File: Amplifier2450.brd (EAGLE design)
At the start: 39.4 x 35.5 mm, 25 parts, among them IC1 7805DT, Q1 P-KANAL_MOSFET_, X1 SMA-142-0701-801/806, X2 SMA-142-0701-801/806

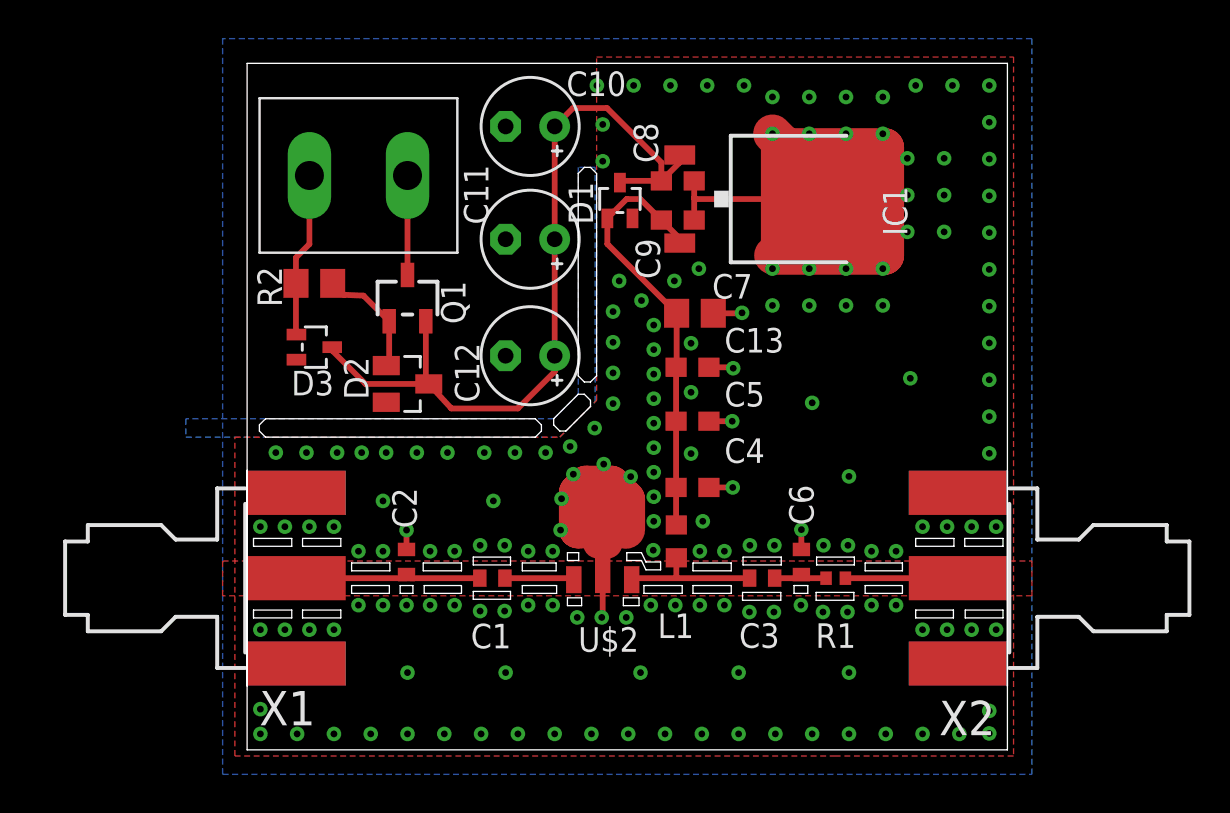
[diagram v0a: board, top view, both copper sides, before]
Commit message: (Tobias): started to apply changes from robert 1st meeting
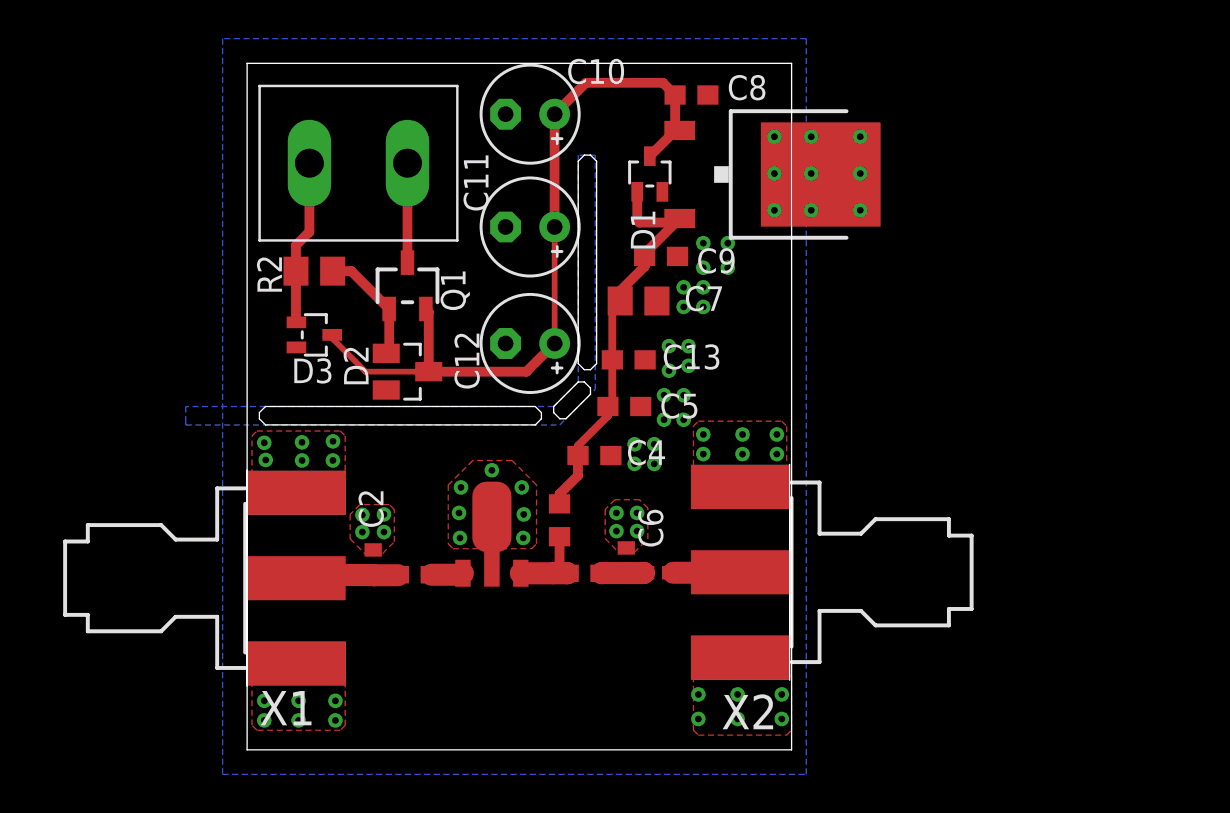
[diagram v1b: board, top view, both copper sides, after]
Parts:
- C13: value 47n -> 22n
- moved X2 11.3 mm to (28.1, 9.19)
- moved R1 9.20 mm to (21.3, 9.17)
- moved C3 9.20 mm to (17.5, 9.14)
- moved C6 9.07 mm to (19.6, 9.80)
- moved L1 6.14 mm to (16.2, 11.9)
- moved U$2 5.75 mm to (12.7, 11.1)
- moved C4 5.34 mm to (18.0, 15.2)
- moved C8 4.50 mm to (23.0, 33.9)
- moved C1 4.02 mm to (8.69, 9.07)
- moved C5 3.61 mm to (19.5, 17.8)
- moved C13 3.32 mm to (19.8, 20.2)
- moved C7 2.99 mm to (20.3, 23.2)
- moved D1 2.07 mm to (20.9, 29.8)
- moved C9 2.07 mm to (21.4, 25.6)
- moved C2 1.73 mm to (6.53, 9.70)
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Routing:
- net GND: track 58.0 -> 8.54 mm, vias 175 -> 59
- net N$2: track 9.75 -> 5.78 mm
- net N$1: track 7.19 -> 4.79 mm
- net +15V: track 41.8 -> 39.4 mm
- net N$5: track 5.82 -> 3.48 mm
- net N$3: track 3.60 -> 1.66 mm
- net +5V: track 22.6 -> 20.9 mm
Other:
- board size 39.4 x 35.5 mm -> 28.2 x 35.5 mm
- board text added: "?????????? Can we use a different width for the power line, so that it has a different impedance and RF will not go up the power line because it would be reflected."
- board text removed: "Lots of vias around the DC-DC Converter gound. This will not only increase the electrical conductance, but also the thermal one. Making use of both ground planes and effectivelly useing them as a heat sink."
- board text removed: "Some random vias in the middle of larger ground planes to make sure that there is no potential difference and the ground is well defined"
- board text removed: "Use thermals around the signal connectors/pads to minimize thermal coupling with other devices"
- board text removed: "Vias at the outer edges intended as shielding from external electro magnetic fields"

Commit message: (Tobias): halfway applied Roberts feedback
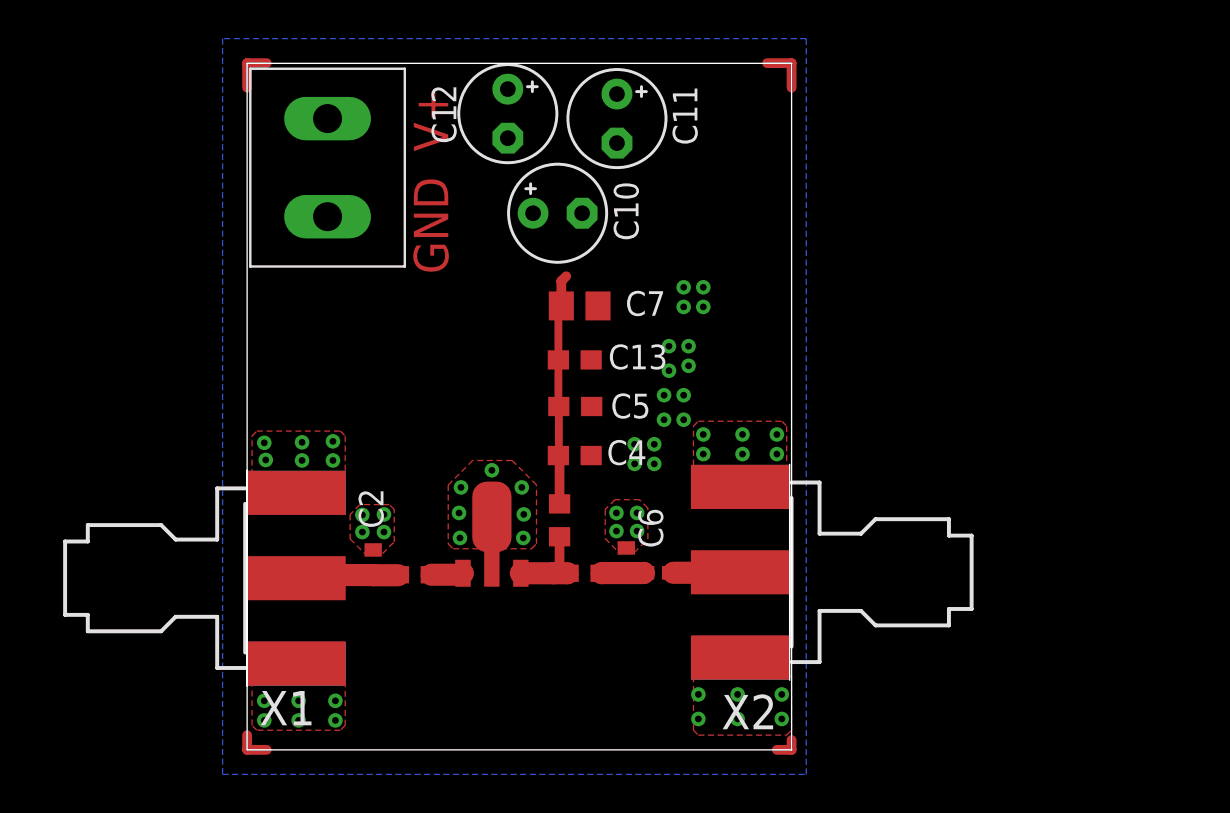
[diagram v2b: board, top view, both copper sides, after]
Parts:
- removed C8: 330n, rcl:C0603
- removed C9: 100n, rcl:C0603
- removed D1, D3: SCHOTTKY_DIODE_, own_htl3r-discrete-1:SOT323
- removed D2: 5,1V, diode:SOT23
- removed IC1: 7805DT, linear:TO252
- removed Q1: P-KANAL_MOSFET_, own_htl3r-discrete-1:SOT346-R
- removed R2: 4k7, rcl:R0805
- C3: value 20p -> 15p
- L1: value 15n -> 72nH
- moved C12 12.0 mm to (13.5, 32.9), turned to 270 degrees
- moved C11 7.19 mm to (19.2, 32.7), turned to 270 degrees
- moved C10 5.32 mm to (16.1, 27.8), turned to 0 degrees
- moved C7 3.06 mm to (17.2, 23.0)
- moved C13 2.79 mm to (17.0, 20.2)
- moved C5 2.54 mm to (17.0, 17.8)
- moved U$1 1.62 mm to (4.17, 30.1), turned to 90 degrees
- moved C4 1.02 mm to (17.0, 15.2)
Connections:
- removed net +15V: C10.+, C11.+, C12.+, C8.1, D1.3, D2.3, D3.3, IC1.1, Q1.2
- removed net N$6: Q1.3, U$1.P$2
- removed net N$7: D2.1, Q1.1, R2.2
- net +5V: now also C10.+, C11.+, C12.+, U$1.P$2; no longer C9.1, D1.1, IC1.2
- net GND: no longer C8.2, C9.2, D3.1, IC1.3, R2.1
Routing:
- net +15V: track 39.4 -> 0.00 mm
- net +5V: track 20.9 -> 12.0 mm
- net GND: track 8.54 -> 0.00 mm, vias 59 -> 55
- net N$7: track 6.10 -> 1.27 mm
- net N$6: track 5.15 -> 1.78 mm
- net N$8: track 0.00 -> 2.54 mm, vias 1 -> 0
- net N$9: track 0.00 -> 2.29 mm, vias 1 -> 0
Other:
- outline, holes or cut-outs redrawn
- board text added: "GND"
- board text added: "V+"

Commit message: (Juanka): Updated PCB
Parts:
- moved C10 1.14 mm to (17.1, 27.3)
- moved C11 0.58 mm to (19.7, 32.8), turned to 90 degrees
- moved C12 0.56 mm to (14.0, 32.8), turned to 0 degrees
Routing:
- net +5V: track 12.0 -> 36.3 mm
- net GND: track 0.00 -> 1.60 mm

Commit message: (Tobias): added documentation to the current design, explaining why certain parts and decisions have been made
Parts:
- moved C12 0.20 mm to (13.9, 32.6), turned to 90 degrees
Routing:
- net +5V: track 36.3 -> 37.4 mm
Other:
- board text added: "Multiple Vias to ground to reduce resistance and inductance of the vias"
- board text removed: "Cutout between power connector and amplifier. The Ground and power lines shall be defined primaraly by the analoge DC-DC Converter. The powerlines shall only connect in a single star point"
- board text removed: "Cutouts around the signal line to minimize dielectric losses in the PCB material. According to my manufacturer clearance of >0.2mm around cutouts is required. Currently 0.25mm is used"

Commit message: (Tobias): made finishing touches to the design
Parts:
- removed C10, C11, C12: 10u, rcl:E2,5-5
- C1, C2, C3, C6: device rcl:C0402 -> rcl:C0603
- L1: device own_htl3r-discrete-1:R_SMD0603 -> rcl:C0603
- R1: device rcl:R0402 -> rcl:C0603
- moved U$1 4.62 mm to (2.90, 25.7)
- moved R1 3.71 mm to (25.0, 9.19)
- moved X2 3.68 mm to (31.8, 9.22)
- moved C6 2.95 mm to (22.1, 8.26), turned to 270 degrees
- moved C3 1.73 mm to (19.2, 9.14)
- moved C4 1.27 mm to (18.2, 15.2)
- moved X1 1.27 mm to (-1.27, 8.89)
- moved L1 1.27 mm to (17.4, 11.9)
- moved U$2 1.27 mm to (13.9, 11.1)
- moved C7 0.80 mm to (16.5, 22.7), turned to 180 degrees
- moved C1 0.63 mm to (9.32, 9.07)
- moved C2 0.63 mm to (6.53, 10.3)
- moved C13 0.63 mm to (16.5, 20.6), turned to 180 degrees
- moved C5 0.46 mm to (16.5, 17.8), turned to 180 degrees
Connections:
- net +5V: no longer C10.+, C11.+, C12.+
- net GND: no longer C10.-, C11.-, C12.-
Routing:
- net +5V: track 37.4 -> 28.3 mm, vias 0 -> 1
- net GND: track 1.60 -> 4.65 mm, vias 55 -> 47
- net N$13: track 0.00 -> 2.69 mm
- net N$12: track 0.00 -> 2.54 mm
- net N$14: track 0.00 -> 2.54 mm
- net N$4: track 2.35 -> 4.80 mm
- net N$2: track 5.78 -> 7.74 mm
- net N$3: track 1.66 -> 3.39 mm
- net N$7: track 1.27 -> 2.67 mm
- net N$16: track 0.00 -> 1.27 mm
- net N$15: track 0.00 -> 1.24 mm
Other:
- board size 28.2 x 35.5 mm -> 33.1 x 31.1 mm
- board text added: "* Power line width at 12mil resulting Impedance is ~98Ohm * Power Reflectance to the signal line is about 10% = ((Z_s - Z_p) / (Z_s - Z_p))^2 * Heat increase of the powerline at 130mA will be less than 2 Kelvin"
- board text added: "Disable thermals around pads and vias, because they would introduce additional small wire inductors."
- board text added: "Have power lines close to each other to reduce noise captured in their spanning area"
- board text added: "Measurements are im mm"
- board text added: "Multiple vias on C4 and C5, event though they are only at DC, to reduce the inductive effects because they have very small capazitive values"
- board text added: "Spread Vias around C6 for sliding"
- board text removed: "?????????? Can we use a different width for the power line, so that it has a different impedance and RF will not go up the power line because it would be reflected."
- board text removed: "GND"
- board text removed: "Starpoint of the power planes/lines to minimize potential loop area."
- board text removed: "V+"
